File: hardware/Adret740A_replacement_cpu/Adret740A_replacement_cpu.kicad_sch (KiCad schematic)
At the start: 7 parts, among them J1 PANNEAU AVANT 2x13, J2 B1 BUS INSTRUMENTS

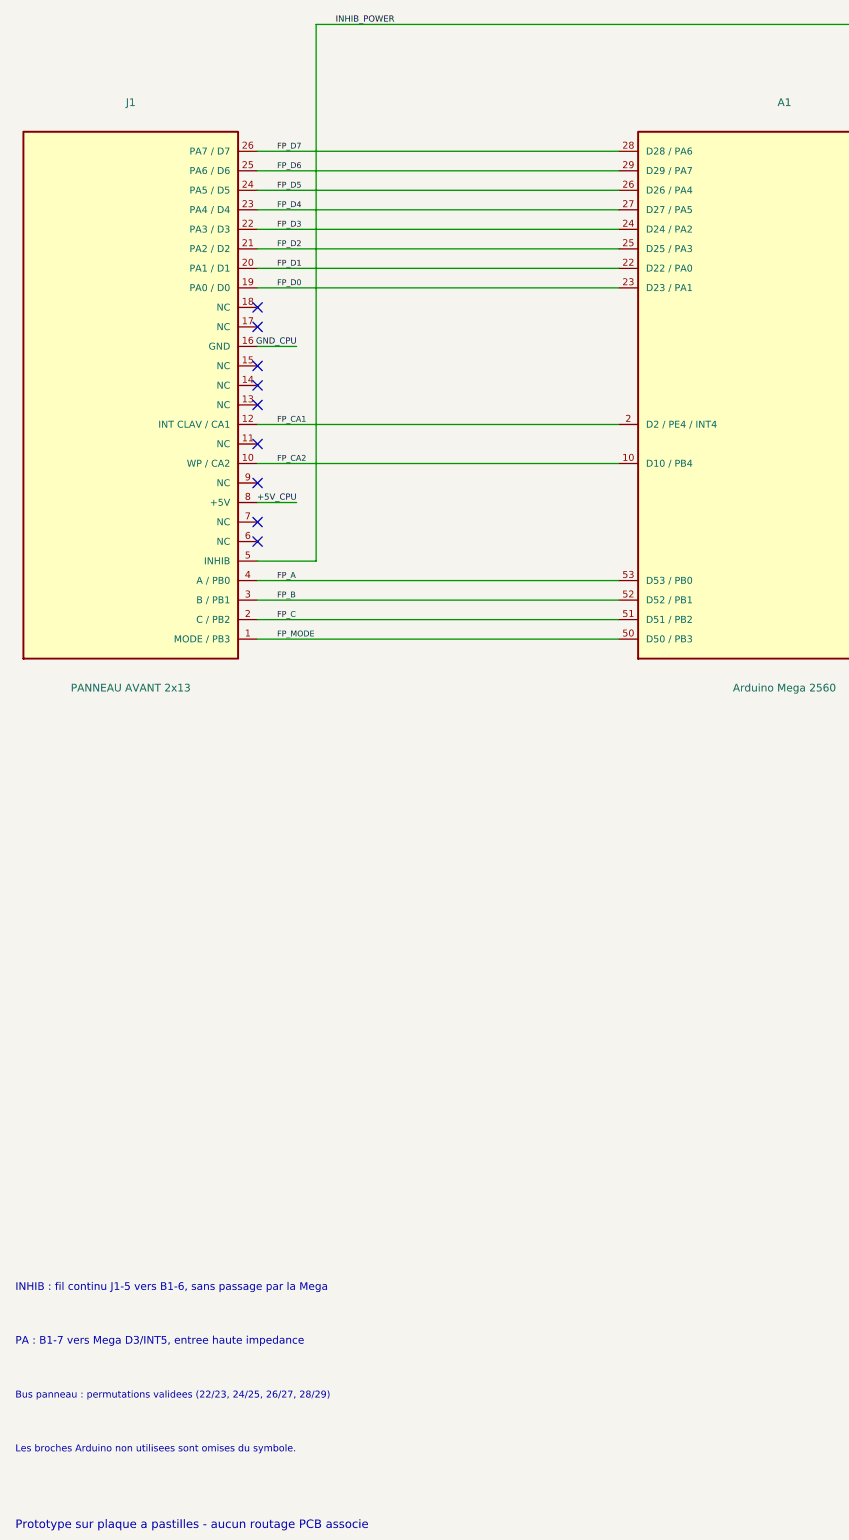
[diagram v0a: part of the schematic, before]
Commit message: Reverse front-panel harness mapping
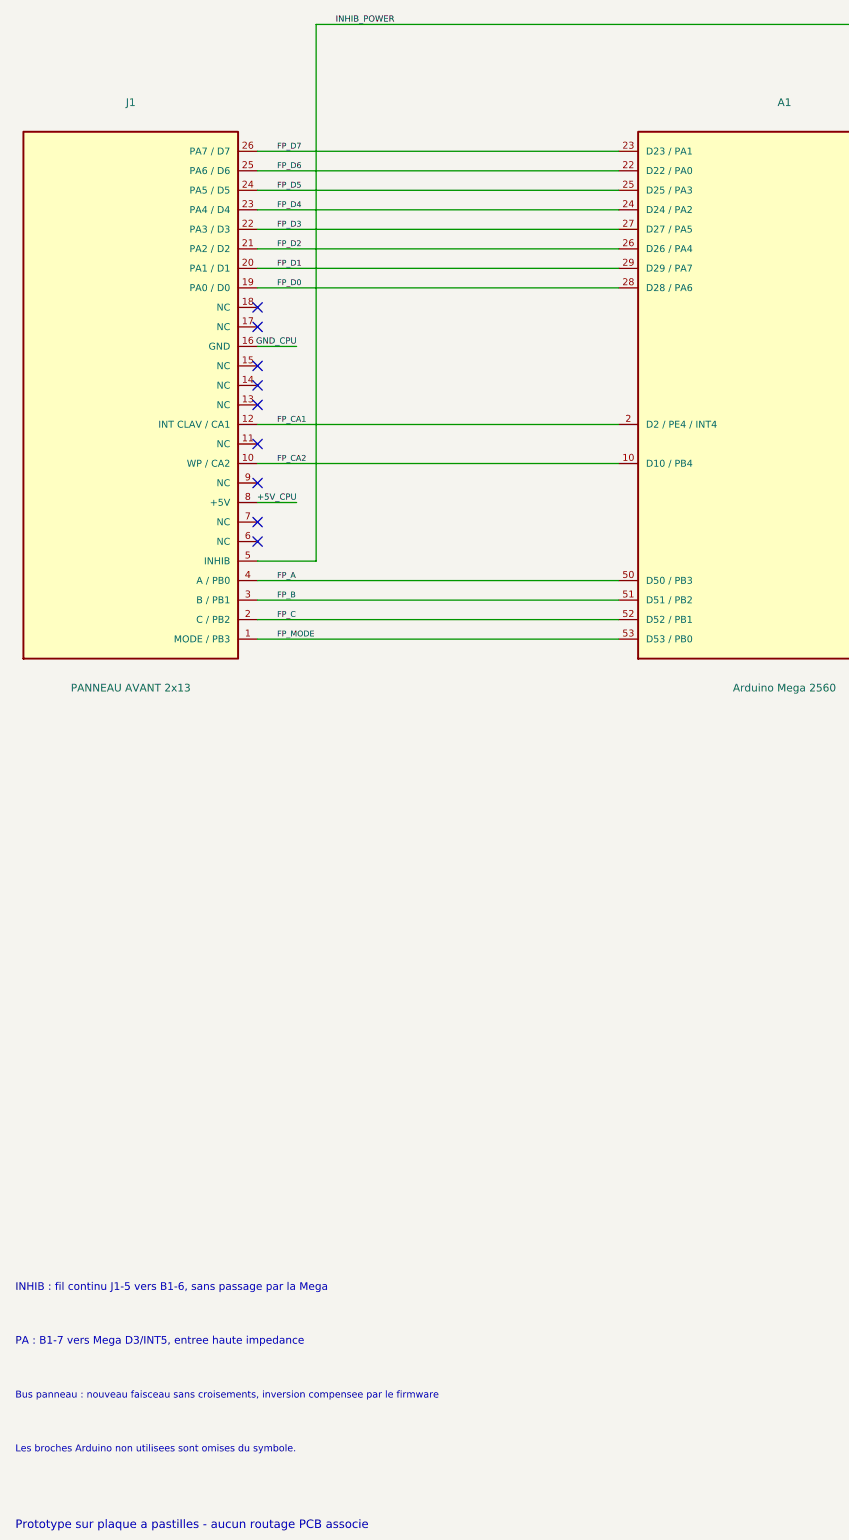
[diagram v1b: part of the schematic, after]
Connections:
- net FP_A: now also A1.50 (D50 / PB3); no longer A1.53 (D53 / PB0)
- net FP_B: now also A1.51 (D51 / PB2); no longer A1.52 (D52 / PB1)
- net FP_C: now also A1.52 (D52 / PB1); no longer A1.51 (D51 / PB2)
- net FP_D0: now also A1.28 (D28 / PA6); no longer A1.23 (D23 / PA1)
- net FP_D1: now also A1.29 (D29 / PA7); no longer A1.22 (D22 / PA0)
- net FP_D2: now also A1.26 (D26 / PA4); no longer A1.25 (D25 / PA3)
- net FP_D3: now also A1.27 (D27 / PA5); no longer A1.24 (D24 / PA2)
- net FP_D4: now also A1.24 (D24 / PA2); no longer A1.27 (D27 / PA5)
- net FP_D5: now also A1.25 (D25 / PA3); no longer A1.26 (D26 / PA4)
- net FP_D6: now also A1.22 (D22 / PA0); no longer A1.29 (D29 / PA7)
- net FP_D7: now also A1.23 (D23 / PA1); no longer A1.28 (D28 / PA6)
- net FP_MODE: now also A1.53 (D53 / PB0); no longer A1.50 (D50 / PB3)
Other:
- note added: "Bus panneau : nouveau faisceau sans croisements, inversion compensee par le firmware"
- note removed: "Bus panneau : permutations validees (22/23, 24/25, 26/27, 28/29)"
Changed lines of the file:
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@@
     )
   )
-  (text "Bus panneau : permutations validees (22/23, 24/25, 26/27, 28/29)"
+  (text "Bus panneau : nouveau faisceau sans croisements, inversion compensee par le firmware"
     (exclude_from_sim no)
     (at 18 221 0)
